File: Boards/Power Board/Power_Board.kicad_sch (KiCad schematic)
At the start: 31 parts, among them J1 Conn_01x02, U1 LM22678TJ-5, U2 LM22678TJ-5

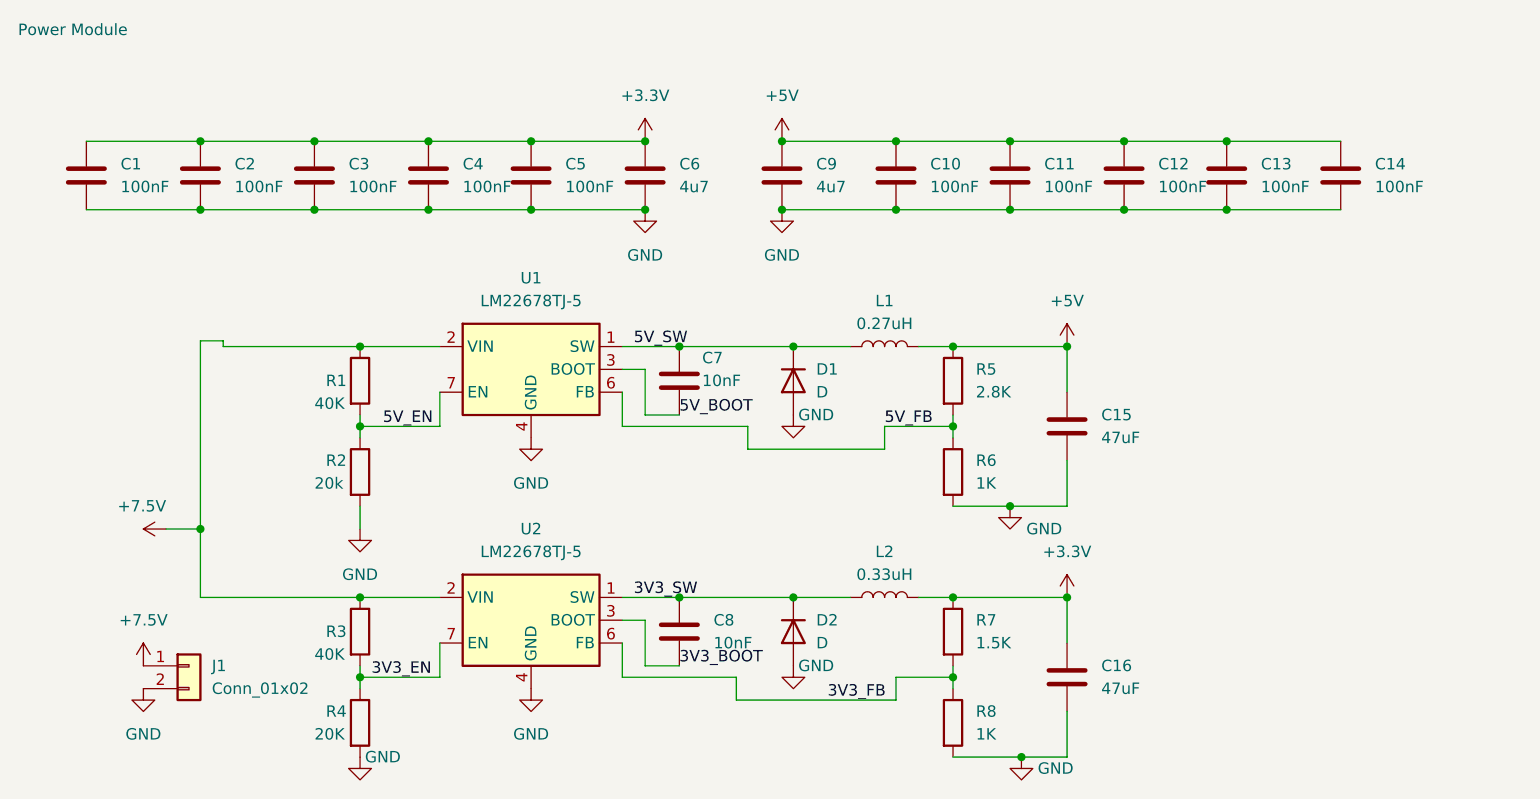
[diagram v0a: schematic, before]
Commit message: power board connectors and ERC changes
reeeeeeeeeeeeeeeeeeeee
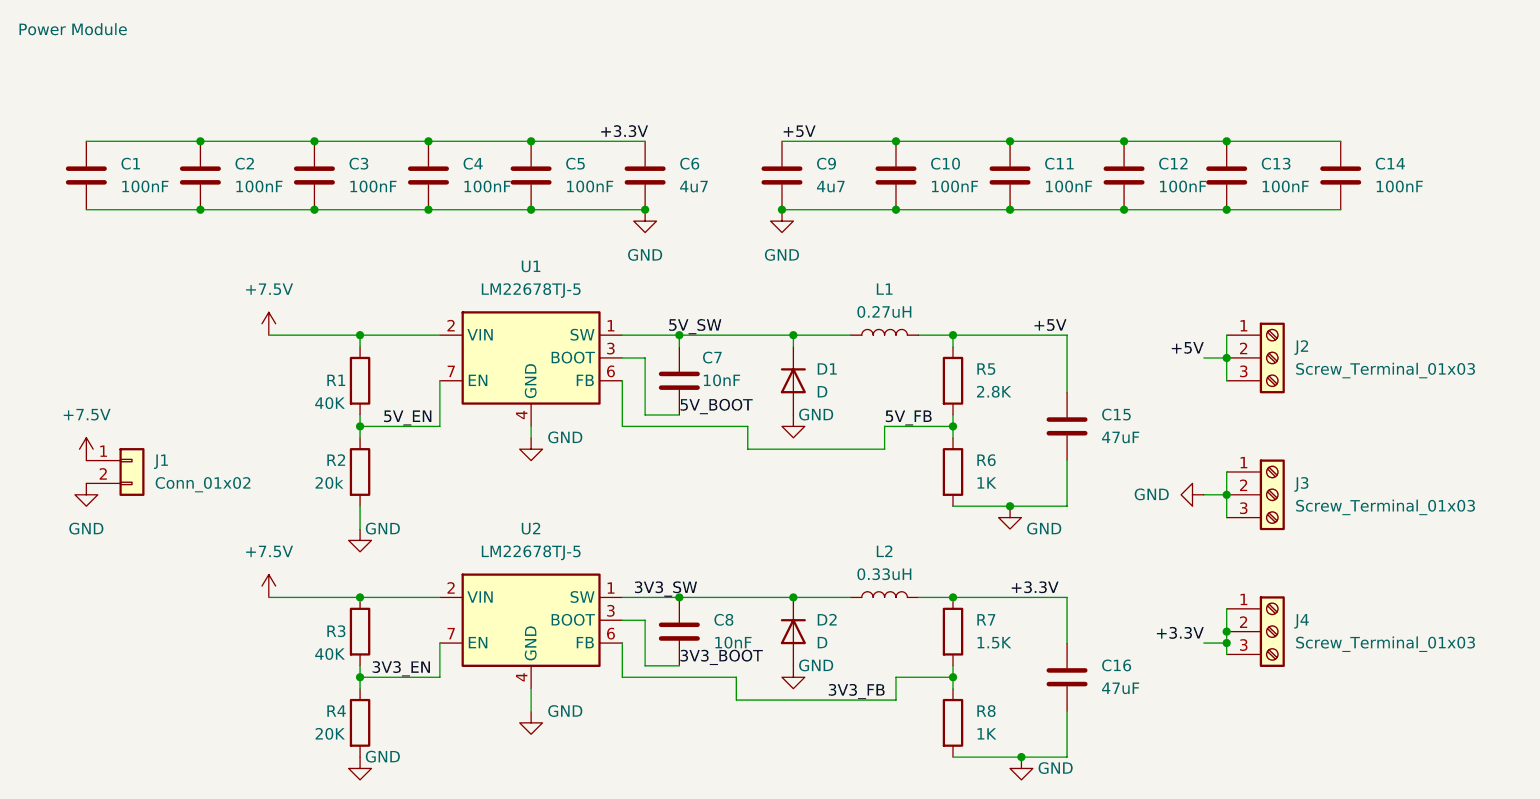
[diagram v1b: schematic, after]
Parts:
- added J2, J3, J4: Screw_Terminal_01x03, Connector_PinSocket_2.54mm:PinSocket_1x03_P2.54mm_Vertical, symbol Connector:Screw_Terminal_01x03
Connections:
- net +3.3V: now also J4.1 (Pin_1), J4.2 (Pin_2), J4.3 (Pin_3)
- net +5V: now also J2.1 (Pin_1), J2.2 (Pin_2), J2.3 (Pin_3)
- net GND: now also J3.1 (Pin_1), J3.2 (Pin_2), J3.3 (Pin_3)
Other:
- moved on the sheet: J1, L1, U1

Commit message: added pwr_flags to resolve errors
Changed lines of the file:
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@@
   (junction (at 153.67 29.21) (diameter 0) (color 0 0 0 0)
   )
+  (junction (at 63.5 80.01) (diameter 0) (color 0 0 0 0)
+  )
   (junction (at 92.71 80.01) (diameter 0) (color 0 0 0 0)
   )
@@
   (junction (at 153.67 85.09) (diameter 0) (color 0 0 0 0)
   )
+  (junction (at 76.2 90.17) (diameter 0) (color 0 0 0 0)
+  )
   (junction (at 153.67 68.58) (diameter 0) (color 0 0 0 0)
   )
@@
     (stroke (width 0) (type default))
   )
-  (wire (pts (xy 57.15 80.01) (xy 66.04 80.01))
+  (wire (pts (xy 57.15 80.01) (xy 63.5 80.01))
     (stroke (width 0) (type default))
   )
@@
   )
   (wire (pts (xy 57.15 87.63) (xy 57.15 88.9))
+    (stroke (width 0) (type default))
+  )
+  (wire (pts (xy 63.5 80.01) (xy 66.04 80.01))
     (stroke (width 0) (type default))
   )
@@
     )
   )
+  (symbol (lib_id "power:PWR_FLAG") (at 76.2 90.17 270) (unit 1)
+    (in_bom yes) (on_board yes) (dnp no) (fields_autoplaced)
+    (property "Reference" "#FLG02" (at 78.105 90.17 0)
+      (effects (font (size 1.27 1.27)) hide)
+    )
+    (property "Value" "PWR_FLAG" (at 80.01 90.17 90)
+      (effects (font (size 1.27 1.27)) (justify left))
+    )
+    (property "Footprint" "" (at 76.2 90.17 0)
+      (effects (font (size 1.27 1.27)) hide)
+    )
+    (property "Datasheet" "~" (at 76.2 90.17 0)
+      (effects (font (size 1.27 1.27)) hide)
+    )
+    (pin "1")
+    (instances
+      (project "Power_Board"
+        (path "/9481fcf2-0a3c-4e9b-839e-2ff680324092"
+          (reference "#FLG02") (unit 1)
+        )
+      )
+    )
+  )
   (symbol (lib_id "power:GND") (at 76.2 62.23 0) (unit 1)
     (in_bom yes) (on_board yes) (dnp no)
@@
         )
       )
+    )
+  )
+  (symbol (lib_id "power:PWR_FLAG") (at 63.5 80.01 0) (unit 1)
+    (in_bom yes) (on_board yes) (dnp no) (fields_autoplaced)
+    (property "Reference" "#FLG01" (at 63.5 78.105 0)
+      (effects (font (size 1.27 1.27)) hide)
+    )
+    (property "Value" "PWR_FLAG" (at 63.5 74.93 0)
+      (effects (font (size 1.27 1.27)))
+    )
+    (property "Footprint" "" (at 63.5 80.01 0)
+      (effects (font (size 1.27 1.27)) hide)
+    )
+    (property "Datasheet" "~" (at 63.5 80.01 0)
+      (effects (font (size 1.27 1.27)) hide)
+    )
+    (pin "1")
+    (instances
+      (project "Power_Board"
+        (path "/9481fcf2-0a3c-4e9b-839e-2ff680324092"
+          (reference "#FLG01") (unit 1)
+        )
+      )
